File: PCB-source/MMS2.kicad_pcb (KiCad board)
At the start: 2 copper layers, 90 x 50 mm, 194 parts, among them J1 86093488324755V1LF, J2 AMASS XT60, J3 Programming header, J7 AMASS XT60, J8 RJ45_LED_Shielded, J800 USB_C_Receptacle_USB2.0_16P, J9 RJ45_LED_Shielded, Q2 AO3400A, Q3 AO3400A, Q5 AO3400A, Q6 AO3400A, Q7 AO3400A, Q700 MMST3904, SW1 BOOT, SW2 RESET, SW5 SW_DIP_x02, U1 STM32F405RGTx, U2 LMR36520ADDAR, U3 TPD2EUSB30DRTR-TP, U301 TPS563200, U302 CH334P, U4 TPD2EUSB30DRTR-TP, U401 TPD2EUSB30DRTR-TP, U5 LM74700, U500 TJA1044GTK_3Z, U501 TJA1044GTK_3Z, U6 AT24C256C, U700 STM32F103CBTx, U801 FSUSB42UMX, X1 X32258MOB4SI, X2 Q13FC1350000400, Y700 Crystal_GND24, Y900 Crystal_GND24

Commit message: ch32
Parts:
- added J4: Conn_01x16_Socket, Connector_PinSocket_2.54mm:PinSocket_1x16_P2.54mm_Vertical, F.Cu at (161.0, 89.8)
- moved H1 182.1 mm to (114.8, 146.8)
- moved H3 182.1 mm to (114.8, 154.0)
- moved H2 180.9 mm to (3.08, 3.08)
- moved R16 38.0 mm to (151.7, 151.8)
- moved R17 38.0 mm to (161.7, 149.2)
- moved R18 38.0 mm to (161.7, 151.2)
- moved R19 38.0 mm to (161.7, 150.2)
- moved R20 38.0 mm to (161.7, 152.2)
- moved R21 38.0 mm to (161.7, 154.2)
- moved R22 38.0 mm to (161.7, 153.2)
- moved U6 38.0 mm to (156.4, 151.7)
- moved R52 5.18 mm to (95.5, 120.7)
- moved R55 4.74 mm to (154.6, 121.2), turned to 180 degrees
- moved U1 4.52 mm to (134.0, 112.5)
- moved X1 4.28 mm to (124.5, 110.1)
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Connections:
- J1 pad A1: /Interboard_connector/Chainbus.SDA -> unconnected-(J1-PadA1)
- J1 pad A10: /Interboard_connector/Chainbus_UART_addr2 -> BRD_VIN
- J1 pad A11: /Interboard_connector/Chainbus.MISO -> BRD_VIN
- J1 pad A12: /Interboard_connector/Chainbus.MOSI -> BRD_VIN
- J1 pad A13: /Interboard_connector/Chainbus.SCK -> BRD_VIN
- J1 pad A14: /Interboard_connector/Chainbus_SPI_CS0 -> GND
- J1 pad A15: /Interboard_connector/Chainbus_SPI_CS1 -> +5V
- J1 pad A16: /Interboard_connector/Chainbus_SPI_CS2 -> +3V3
- J1 pad A2: /Interboard_connector/Chainbus.SCL -> unconnected-(J1-PadA2)
- J1 pad A3: /Interboard_connector/Chainbus_I2C_addr0 -> unconnected-(J1-PadA3)
- J1 pad A4: /Interboard_connector/Chainbus_I2C_addr1 -> unconnected-(J1-PadA4)
- J1 pad A5: /Interboard_connector/Chainbus_I2C_addr2 -> unconnected-(J1-PadA5)
- J1 pad A6: /Interboard_connector/Chainbus.RX -> GND
- J1 pad A7: /Interboard_connector/Chainbus.TX -> GND
- J1 pad A8: /Interboard_connector/Chainbus_UART_addr0 -> GND
- J1 pad A9: /Interboard_connector/Chainbus_UART_addr1 -> GND
- J1 pad B1: unconnected-(J1-PadB1) -> /Interboard_connector/Chainbus.SDA
- J1 pad B10: GND -> /Interboard_connector/Chainbus_UART_addr2
- J1 pad B11: unconnected-(J1-PadB11) -> /Interboard_connector/Chainbus.MISO
- J1 pad B12: unconnected-(J1-PadB12) -> /Interboard_connector/Chainbus.MOSI
- J1 pad B13: GND -> /Interboard_connector/Chainbus.SCK
- J1 pad B14: GND -> /Interboard_connector/Chainbus_SPI_CS0
- J1 pad B15: GND -> /Interboard_connector/Chainbus_SPI_CS1
- J1 pad B16: GND -> /Interboard_connector/Chainbus_SPI_CS2
- J1 pad B2: unconnected-(J1-PadB2) -> /Interboard_connector/Chainbus.SCL
- J1 pad B3: unconnected-(J1-PadB3) -> /Interboard_connector/Chainbus_I2C_addr0
- J1 pad B4: unconnected-(J1-PadB4) -> /Interboard_connector/Chainbus_I2C_addr1
- J1 pad B5: unconnected-(J1-PadB5) -> /Interboard_connector/Chainbus_I2C_addr2
- J1 pad B6: unconnected-(J1-PadB6) -> /Interboard_connector/Chainbus.RX
- J1 pad B7: GND -> /Interboard_connector/Chainbus.TX
- J1 pad B8: GND -> /Interboard_connector/Chainbus_UART_addr0
- J1 pad B9: GND -> /Interboard_connector/Chainbus_UART_addr1
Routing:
- net /CAN auto terminator/CAN2.-: track 119.9 -> 81.4 mm, vias 3 -> 2
- net /CAN auto terminator/CAN2.+: track 118.5 -> 80.5 mm, vias 3 -> 2
- net /MCU/USB_MCU.D+: track 37.6 -> 0.97 mm
- net /MCU/USB_MCU.D-: track 36.6 -> 0.97 mm
- net /MMS_CONNECTOR_DOWNSTREAM/USB_MMS_CONN.D-: track 81.2 -> 61.1 mm
- net /MMS_CONNECTOR_DOWNSTREAM/USB_MMS_CONN.D+: track 79.3 -> 60.7 mm
- net /CAN auto terminator/CAN1.+: track 102.7 -> 85.4 mm, vias 3 -> 2
- net /CAN auto terminator/CAN1.-: track 101.9 -> 84.7 mm, vias 3 -> 2
- net Net-(J9-Pad10): track 4.02 -> 0.00 mm
- net Net-(J8-Pad12): track 2.89 -> 0.00 mm
- net Net-(J8-Pad10): track 3.48 -> 5.11 mm
- net /MMS_CONNECTOR_UPSTREAM/USB_MMS_CONN.D+: track 17.1 -> 16.4 mm
- net GND: track 25.1 -> 25.5 mm, vias 106 -> 88

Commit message: Component placement done
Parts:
- removed C405, C420, C421: 100nF, PCM_JLCPCB:C_0402
- removed R400: 1.2kΩ, PCM_JLCPCB:R_0402
- removed R408: 220Ω, PCM_JLCPCB:R_0402
- removed R409: 100Ω, PCM_JLCPCB:R_0402
- removed SW5: SW_DIP_x02, Button_Switch_SMD:SW_DIP_SPSTx02_Slide_6.7x6.64mm_W8.61mm_P2.54mm_LowProfile
- removed TP302, TP700, TP701: TestPoint, TestPoint:TestPoint_Pad_D1.0mm
- added C33: 100nF, PCM_JLCPCB:C_0402, F.Cu at (112.6, 105.8)
- added D4: Red, PCM_JLCPCB:D_0603, F.Cu at (115.4, 112.6)
- added J5: Conn_01x03_Pin, Connector_PinHeader_1.27mm:PinHeader_1x03_P1.27mm_Vertical, B.Cu at (108.1, 110.5)
- added R23: 220Ω, PCM_JLCPCB:R_0402, F.Cu at (142.6, 146.1)
- added R24: 220Ω, PCM_JLCPCB:R_0402, F.Cu at (115.1, 115.2)
- added U7: CH32V003FxUx, Package_DFN_QFN:QFN-20-1EP_3x3mm_P0.4mm_EP1.65x1.65mm, F.Cu at (113.6, 108.5)
- J3: moved to B.Cu
- moved H2 180.3 mm to (103.1, 153.1)
- moved R703 126.3 mm to (109.1, 92.0), turned to 180 degrees
- moved C700 125.8 mm to (111.2, 99.5), turned to -90 degrees
- moved R407 111.0 mm to (144.8, 145.7)
- moved R402 102.9 mm to (139.4, 116.6), turned to -45 degrees
- moved C425 102.1 mm to (127.2, 103.7), turned to 90 degrees
- moved R401 101.4 mm to (140.8, 115.2), turned to 135 degrees
- moved C422 101.3 mm to (129.8, 119.8), turned to 135 degrees
- moved C426 100.6 mm to (128.1, 103.7), turned to 90 degrees
- moved C410 100.5 mm to (140.1, 115.9), turned to -45 degrees
- moved C402 98.8 mm to (125.1, 109.5), turned to 45 degrees
- moved C424 97.3 mm to (133.0, 103.7), turned to 90 degrees
- moved R406 96.1 mm to (145.9, 104.4)
- moved C400 96.1 mm to (127.7, 105.1), turned to 180 degrees
- moved R403 94.6 mm to (145.9, 108.8), turned to 180 degrees
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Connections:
- J1 pad C10: /Interboard_connector/Altmode10 -> /Interboard_connector/Altmode14
- J1 pad C11: /Interboard_connector/Altmode11 -> /Interboard_connector/Altmode15
- J1 pad C12: /Interboard_connector/Altmode12 -> /Interboard_connector/Altmode7
- J1 pad C13: /Interboard_connector/Altmode13 -> /Interboard_connector/Altmode8
- J1 pad C14: /Interboard_connector/Altmode14 -> /Interboard_connector/Altmode9
- J1 pad C15: /Interboard_connector/Altmode15 -> /Interboard_connector/Altmode10
- J1 pad C7: /Interboard_connector/Altmode7 -> /Interboard_connector/Altmode11
- J1 pad C8: /Interboard_connector/Altmode8 -> /Interboard_connector/Altmode12
- J1 pad C9: /Interboard_connector/Altmode9 -> /Interboard_connector/Altmode13
- U1 pad 10: unconnected-(U1-PC2-Pad10) -> /Interboard_connector/Altmode14
- U1 pad 11: unconnected-(U1-PC3-Pad11) -> /Interboard_connector/Altmode15
- U1 pad 14: unconnected-(U1-PA0-Pad14) -> /Interboard_connector/Altmode7
- U1 pad 15: unconnected-(U1-PA1-Pad15) -> /Interboard_connector/Altmode8
- U1 pad 16: unconnected-(U1-PA2-Pad16) -> /Interboard_connector/Altmode9
- U1 pad 17: unconnected-(U1-PA3-Pad17) -> /Interboard_connector/Altmode10
- U1 pad 21: unconnected-(U1-PA5-Pad21) -> /Interboard_connector/Chainbus_UART_addr2
- U1 pad 22: unconnected-(U1-PA6-Pad22) -> /Interboard_connector/Chainbus_UART_addr0
- U1 pad 23: unconnected-(U1-PA7-Pad23) -> /Interboard_connector/Chainbus_UART_addr1
- U1 pad 24: unconnected-(U1-PC4-Pad24) -> /Interboard_connector/Altmode16
- U1 pad 29: unconnected-(U1-PB10-Pad29) -> /Interboard_connector/Chainbus.SCL
- U1 pad 30: unconnected-(U1-PB11-Pad30) -> /Interboard_connector/Chainbus.SDA
- U1 pad 34: unconnected-(U1-PB13-Pad34) -> /Interboard_connector/Altmode4
- U1 pad 35: unconnected-(U1-PB14-Pad35) -> /Interboard_connector/Altmode5
- U1 pad 36: unconnected-(U1-PB15-Pad36) -> /Interboard_connector/Altmode6
- U1 pad 37: unconnected-(U1-PC6-Pad37) -> /Interboard_connector/Chainbus_SPI_CS0
- U1 pad 38: unconnected-(U1-PC7-Pad38) -> /Interboard_connector/Chainbus_SPI_CS1
- U1 pad 39: unconnected-(U1-PC8-Pad39) -> /Interboard_connector/Chainbus_SPI_CS2
- U1 pad 40: unconnected-(U1-PC9-Pad40) -> /Interboard_connector/Chainbus_I2C_addr2
- U1 pad 41: unconnected-(U1-PA8-Pad41) -> /Interboard_connector/Altmode1
- U1 pad 42: unconnected-(U1-PA9-Pad42) -> /Interboard_connector/Altmode2
- U1 pad 43: unconnected-(U1-PA10-Pad43) -> /Interboard_connector/Altmode3
- U1 pad 50: unconnected-(U1-PA15-Pad50) -> /Interboard_connector/Chainbus_I2C_addr0
- U1 pad 53: unconnected-(U1-PC12-Pad53) -> /Interboard_connector/Chainbus.MOSI
- U1 pad 55: unconnected-(U1-PB3-Pad55) -> /Interboard_connector/Chainbus.SCK
- U1 pad 56: unconnected-(U1-PB4-Pad56) -> /Interboard_connector/Chainbus.MISO
- U1 pad 57: unconnected-(U1-PB5-Pad57) -> /Interboard_connector/Chainbus_I2C_addr1
- U1 pad 59: unconnected-(U1-PB7-Pad59) -> /Interboard_connector/Altmode11
- U1 pad 8: unconnected-(U1-PC0-Pad8) -> /Interboard_connector/Altmode12
- U1 pad 9: unconnected-(U1-PC1-Pad9) -> /Interboard_connector/Altmode13
- U700 pad 12: /STlink-BMprobe/STLINK_TX -> /CH32V003/CH_UART.RX
- U700 pad 13: /STlink-BMprobe/STLINK_RX -> /CH32V003/CH_UART.TX
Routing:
- net /Interboard_connector/Altmode4: track 0.00 -> 54.3 mm
- net /Interboard_connector/Altmode5: track 0.00 -> 49.1 mm
- net /Interboard_connector/Altmode6: track 0.00 -> 44.6 mm
- net /MCU/USB_MCU.D+: track 0.97 -> 40.3 mm
- net /MCU/USB_MCU.D-: track 0.97 -> 39.9 mm
- net /Interboard_connector/Altmode11: track 0.00 -> 27.1 mm
- net /MMS_CONNECTOR_DOWNSTREAM/USB_MMS_CONN.D-: track 61.1 -> 86.5 mm
- net /CAN auto terminator/CAN2.-: track 81.4 -> 106.7 mm, vias 2 -> 3
- net /MMS_CONNECTOR_DOWNSTREAM/USB_MMS_CONN.D+: track 60.7 -> 86.0 mm
- net /CH32V003/CH_UART.TX: track 0.00 -> 23.3 mm, vias 0 -> 2
- net /CAN auto terminator/CAN1.-: track 84.7 -> 107.6 mm, vias 2 -> 3
- net /CAN auto terminator/CAN2.+: track 80.5 -> 101.9 mm, vias 2 -> 3
- net /CAN auto terminator/CAN1.+: track 85.4 -> 104.4 mm, vias 2 -> 3
- net /CH32V003/CH_UART.RX: track 0.00 -> 18.9 mm, vias 0 -> 2
- net +3V3: track 17.7 -> 33.2 mm
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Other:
- board text removed: "21.5khz pi filter or check on vesc forum"

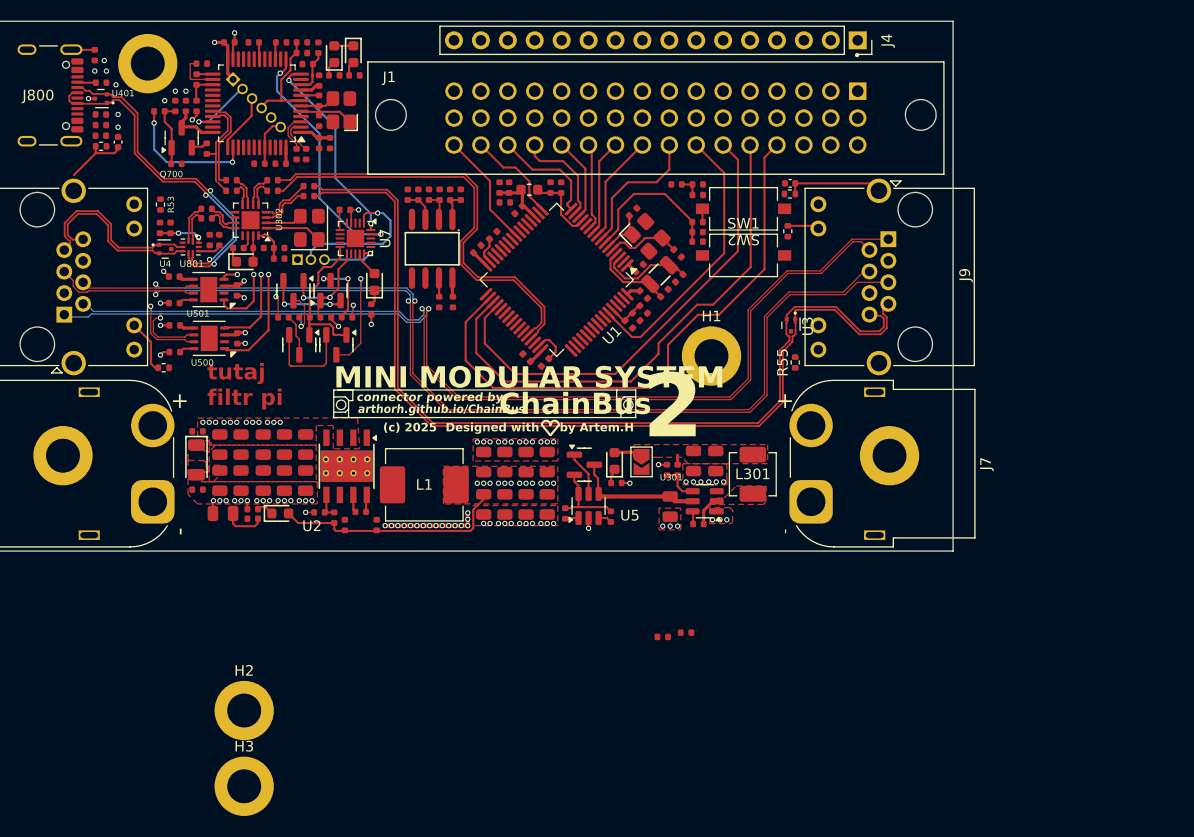
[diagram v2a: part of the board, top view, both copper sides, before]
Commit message: processor connection done
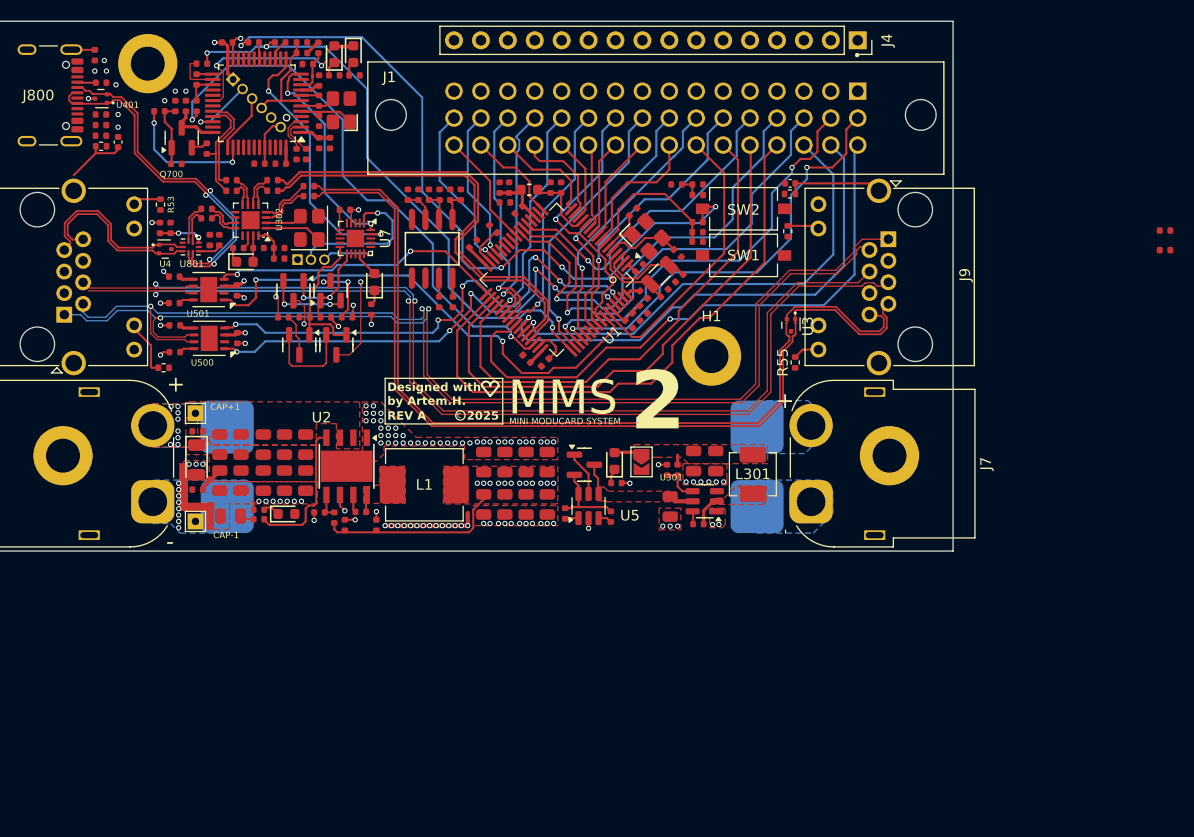
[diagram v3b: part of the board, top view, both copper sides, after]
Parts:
- removed H2, H3: M3 mount, MountingHole:MountingHole_3.2mm_M3_DIN965_Pad
- added BAR1: Bus Bar 5x50mm, BusBar:BusBar-50mm-Red, B.Cu at (155.0, 129.3)
- added BAR2: Bus Bar 5x50mm, BusBar:BusBar-50mm-black, B.Cu at (154.5, 136.8)
- added CAP+1: Capacitor +, TestPoint:TestPoint_THTPad_1.5x1.5mm_Drill0.7mm, F.Cu at (98.5, 125.0)
- added CAP-1: Capacitor -, TestPoint:TestPoint_THTPad_1.5x1.5mm_Drill0.7mm, F.Cu at (98.5, 135.2)
- added NT1: custom net tie, PgndNetTie:Custom, F.Cu at (99.9, 135.7)
- moved R23 61.0 mm to (190.0, 107.8)
- moved R407 57.8 mm to (190.0, 109.6)
- moved C16 0.74 mm to (101.8, 134.7)
- moved C402 0.64 mm to (124.7, 109.0)
- moved C29 0.60 mm to (126.6, 107.6), turned to 135 degrees
- moved D402 0.59 mm to (107.1, 134.5)
- moved R10 0.59 mm to (104.5, 135.0), turned to 180 degrees
- moved R12 0.59 mm to (104.5, 134.1)
- moved C701 0.20 mm to (101.5, 90.0)
- moved C422 0.10 mm to (129.8, 119.9)
- moved R704 0.10 mm to (106.5, 90.0), turned to 180 degrees
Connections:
- J1 pad B1: /Interboard_connector/Chainbus.SDA -> /Interboard_connector/Chainbus.RX
- J1 pad B10: /Interboard_connector/Chainbus_UART_addr2 -> /Interboard_connector/Chainbus_I2C_addr1
- J1 pad B11: /Interboard_connector/Chainbus.MISO -> /Interboard_connector/Chainbus_I2C_addr2
- J1 pad B12: /Interboard_connector/Chainbus.MOSI -> /Interboard_connector/Chainbus_SPI_CS0
- J1 pad B13: /Interboard_connector/Chainbus.SCK -> /Interboard_connector/Chainbus_SPI_CS1
- J1 pad B14: /Interboard_connector/Chainbus_SPI_CS0 -> /Interboard_connector/Chainbus_SPI_CS2
- J1 pad B15: /Interboard_connector/Chainbus_SPI_CS1 -> /Interboard_connector/Chainbus.SCL
- J1 pad B16: /Interboard_connector/Chainbus_SPI_CS2 -> /Interboard_connector/Chainbus.SDA
- J1 pad B2: /Interboard_connector/Chainbus.SCL -> /Interboard_connector/Chainbus.TX
- J1 pad B3: /Interboard_connector/Chainbus_I2C_addr0 -> /Interboard_connector/Chainbus_UART_addr0
- J1 pad B4: /Interboard_connector/Chainbus_I2C_addr1 -> /Interboard_connector/Chainbus_UART_addr1
- J1 pad B5: /Interboard_connector/Chainbus_I2C_addr2 -> /Interboard_connector/Chainbus_UART_addr2
- J1 pad B6: /Interboard_connector/Chainbus.RX -> /Interboard_connector/Chainbus.MISO
- J1 pad B7: /Interboard_connector/Chainbus.TX -> /Interboard_connector/Chainbus.MOSI
- J1 pad B8: /Interboard_connector/Chainbus_UART_addr0 -> /Interboard_connector/Chainbus.SCK
- J1 pad B9: /Interboard_connector/Chainbus_UART_addr1 -> /Interboard_connector/Chainbus_I2C_addr0
- U1 pad 26: unconnected-(U1-PB0-Pad26) -> /MCU/USER_LED_1
- U1 pad 27: unconnected-(U1-PB1-Pad27) -> /MCU/USER_LED_2
- U1 pad 51: unconnected-(U1-PC10-Pad51) -> /Interboard_connector/Chainbus.TX
- U1 pad 52: unconnected-(U1-PC11-Pad52) -> /Interboard_connector/Chainbus.RX
- U7 pad 12: unconnected-(U7-PC5-Pad12) -> (no net)
- U7 pad 13: unconnected-(U7-PC6-Pad13) -> (no net)
- U7 pad 16: unconnected-(U7-PD2-Pad16) -> (no net)
- U7 pad 17: unconnected-(U7-PD3-Pad17) -> (no net)
- U7 pad 18: unconnected-(U7-PD4-Pad18) -> (no net)
- U7 pad 2: unconnected-(U7-PA1-Pad2) -> (no net)
- U7 pad 3: unconnected-(U7-PA2-Pad3) -> (no net)
- U7 pad 5: unconnected-(U7-PD0-Pad5) -> (no net)
- U7 pad 7: unconnected-(U7-PC0-Pad7) -> (no net)
- U7 pad 8: unconnected-(U7-PC1-Pad8) -> (no net)
- U7 pad 9: unconnected-(U7-PC2-Pad9) -> (no net)
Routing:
- net /MCU/SWD.~{RST}: track 1.32 -> 69.5 mm, vias 0 -> 4
- net /MCU/SWD.SWCLK: track 0.00 -> 56.8 mm, vias 0 -> 3
- net /Interboard_connector/Altmode1: track 0.00 -> 56.4 mm, vias 0 -> 1
- net /MCU/SWD.SWDIO: track 0.97 -> 54.1 mm, vias 1 -> 2
- net /Interboard_connector/Altmode2: track 0.00 -> 48.6 mm, vias 0 -> 1
- net /Interboard_connector/Chainbus_UART_addr0: track 0.00 -> 46.0 mm, vias 0 -> 1
- net /Interboard_connector/Altmode3: track 0.00 -> 45.4 mm, vias 0 -> 1
- net /Interboard_connector/Chainbus_UART_addr1: track 0.00 -> 42.7 mm, vias 0 -> 1
- net /Interboard_connector/Chainbus.RX: track 0.00 -> 41.3 mm, vias 0 -> 2
- net /CAN_TR2/CAN.TX: track 6.23 -> 47.0 mm, vias 1 -> 2
- net /CAN_TR1/CAN.RX: track 7.93 -> 48.1 mm, vias 1 -> 6
- net /Interboard_connector/Chainbus.TX: track 0.00 -> 39.4 mm, vias 0 -> 2
- net /CAN_TR1/CAN.TX: track 10.0 -> 45.5 mm, vias 1 -> 6
- net /Interboard_connector/Chainbus_UART_addr2: track 0.00 -> 30.7 mm, vias 0 -> 1
- net /CAN_TR2/CAN.RX: track 1.58 -> 27.9 mm, vias 1 -> 2
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- added copper zone on F.Cu, net /VRM/LMR36520ADDAR/SW
- added copper zone on B.Cu, net BRD_VIN
- added copper zone on In1.Cu, net GND
- added copper zone on B.Cu, net GNDPWR
- added copper zone on F.Cu, net VBUS
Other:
- copper layers 2 -> 4
- board text added: "2025"
- board text added: "Designed with"
- board text added: "MINI MODUCARD SYSTEM"
- board text added: "MMS"
- board text added: "REV A"
- board text added: "Ymin LKME5001J102MF"
- board text added: "by Artem.H."
- board text added: "c"
- board text removed: "(c) 2025"
- board text removed: "Designed with by Artem.H"
- board text removed: "MINI MODULAR SYSTEM"
- board text removed: "tutaj filtr pi"
